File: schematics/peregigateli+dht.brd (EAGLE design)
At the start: 100 x 80 mm, 20 parts

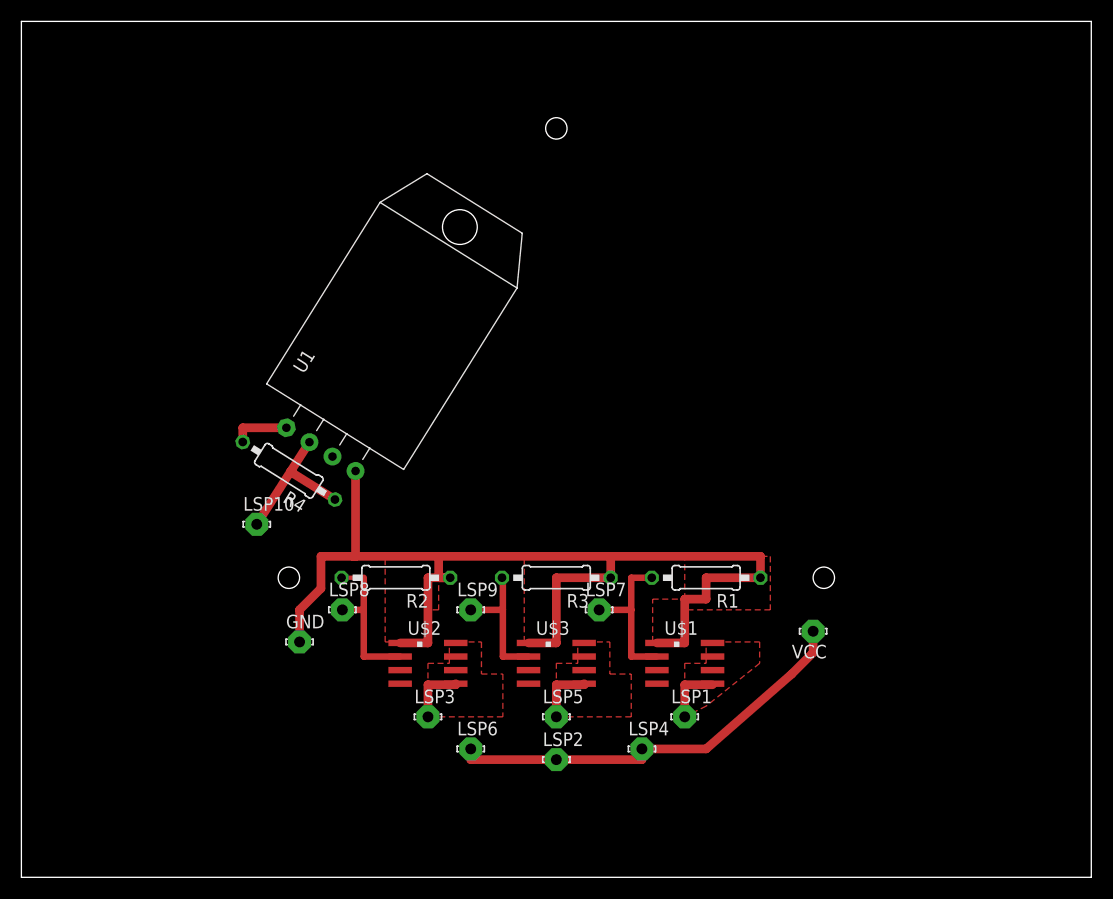
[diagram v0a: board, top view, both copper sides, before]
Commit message: плата с пережигателями
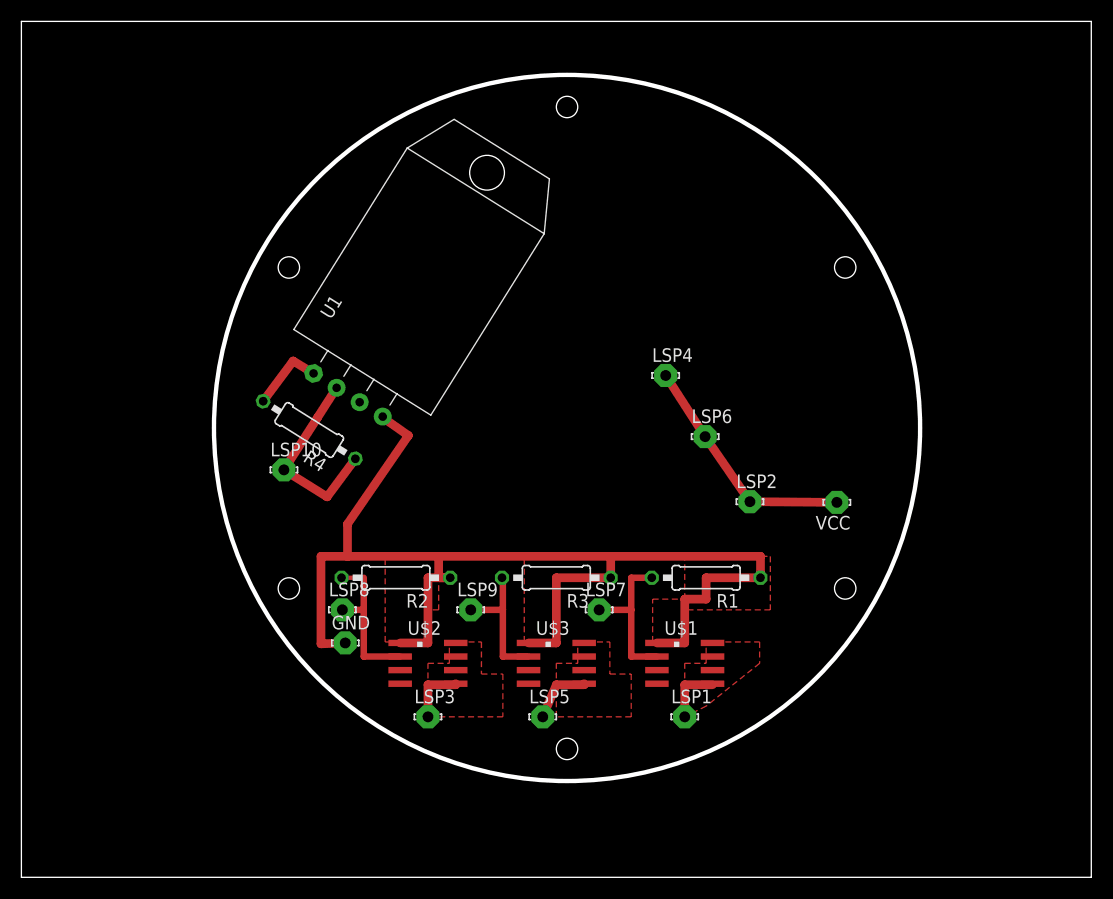
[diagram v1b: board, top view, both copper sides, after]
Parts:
- moved LSP6 36.5 mm to (63.9, 41.2)
- moved LSP4 35.0 mm to (60.2, 46.9)
- moved LSP2 30.1 mm to (68.1, 35.1)
- moved VCC 12.2 mm to (76.2, 35.0)
- moved LSP10 5.68 mm to (24.5, 38.1)
- moved U1 5.68 mm to (30.5, 45.1)
- moved GND 4.27 mm to (30.3, 21.9)
- moved R4 4.26 mm to (26.9, 41.8)
- moved LSP5 1.27 mm to (48.7, 15.0)
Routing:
- net N$2: track 39.5 -> 22.3 mm
- net GND: track 105.3 -> 115.1 mm
- net N$1: track 14.0 -> 18.3 mm
- net N$5: track 5.40 -> 6.92 mm
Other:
- outline, holes or cut-outs redrawn

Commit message: плата на печать
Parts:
- moved LSP4 20.4 mm to (62.1, 67.2)
- moved LSP6 20.3 mm to (70.9, 60.2)
- moved LSP2 15.9 mm to (75.7, 49.1)
- moved VCC 4.49 mm to (79.4, 38.2)
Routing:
- net N$2: track 22.3 -> 34.8 mm
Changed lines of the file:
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@@
 <element name="GND" library="solpad" package="LSP10" value="LSP10" x="30.27" y="21.905"/>
 <element name="LSP1" library="solpad" package="LSP10" value="LSP10" x="62" y="15"/>
-<element name="LSP2" library="solpad" package="LSP10" value="LSP10" x="68.095" y="35.11"/>
+<element name="LSP2" library="solpad" package="LSP10" value="LSP10" x="75.715" y="49.08"/>
 <element name="LSP3" library="solpad" package="LSP10" value="LSP10" x="38" y="15"/>
-<element name="LSP4" library="solpad" package="LSP10" value="LSP10" x="60.22" y="46.905"/>
+<element name="LSP4" library="solpad" package="LSP10" value="LSP10" x="62.125" y="67.225"/>
 <element name="LSP5" library="solpad" package="LSP10" value="LSP10" x="48.73" y="15"/>
-<element name="LSP6" library="solpad" package="LSP10" value="LSP10" x="63.905" y="41.19"/>
+<element name="LSP6" library="solpad" package="LSP10" value="LSP10" x="70.89" y="60.24"/>
 <element name="R1" library="resistor" package="0207/10" value="" x="64" y="28" rot="R180"/>
 <element name="R2" library="resistor" package="0207/10" value="" x="35" y="28" rot="R180"/>
@@
 <element name="U$2" library="elements" package="SOIC-8" value="AO4606" x="38" y="20" rot="R270"/>
 <element name="U$3" library="elements" package="SOIC-8" value="AO4606" x="50" y="20" rot="R270"/>
-<element name="VCC" library="solpad" package="LSP10" value="LSP10" x="76.22" y="35.045" rot="R180"/>
+<element name="VCC" library="solpad" package="LSP10" value="LSP10" x="79.395" y="38.22" rot="R180"/>
 <element name="LSP7" library="solpad" package="LSP10" value="LSP10" x="54" y="25"/>
 <element name="LSP8" library="solpad" package="LSP10" value="LSP10" x="30" y="25"/>
@@
 <contactref element="LSP4" pad="MP"/>
 <contactref element="LSP6" pad="MP"/>
-<wire x1="60.22" y1="46.905" x2="63.905" y2="41.19" width="0.8128" layer="1"/>
-<wire x1="63.905" y1="41.19" x2="68.095" y2="35.11" width="0.8128" layer="1"/>
-<wire x1="68.095" y1="35.11" x2="76.22" y2="35.045" width="0.8128" layer="1"/>
+<wire x1="62.125" y1="67.225" x2="70.89" y2="60.24" width="0.8128" layer="1"/>
+<wire x1="70.89" y1="60.24" x2="75.715" y2="49.08" width="0.8128" layer="1"/>
+<wire x1="75.715" y1="49.08" x2="79.395" y2="38.22" width="0.8128" layer="1"/>
 </signal>
 <signal name="GND">
